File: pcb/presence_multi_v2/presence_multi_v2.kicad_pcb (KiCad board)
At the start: 2 copper layers, 77 x 42 mm, 32 parts, among them IC1 LDL1117S33R, J1 USB_C_Receptacle_USB2.0_16P, J2 TC2050, J3 Conn_01x06_Socket, U3 CH340E, Y1 Wurth 830050789

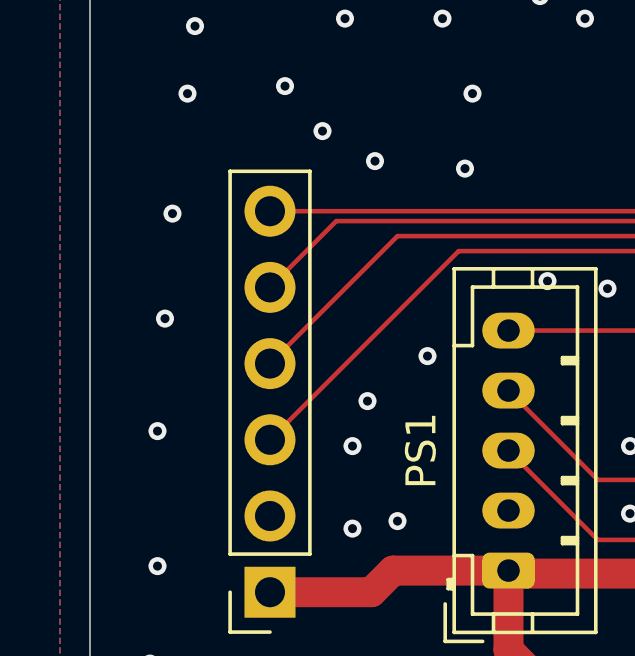
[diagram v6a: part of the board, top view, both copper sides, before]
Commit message: added info on components to a silkscreen
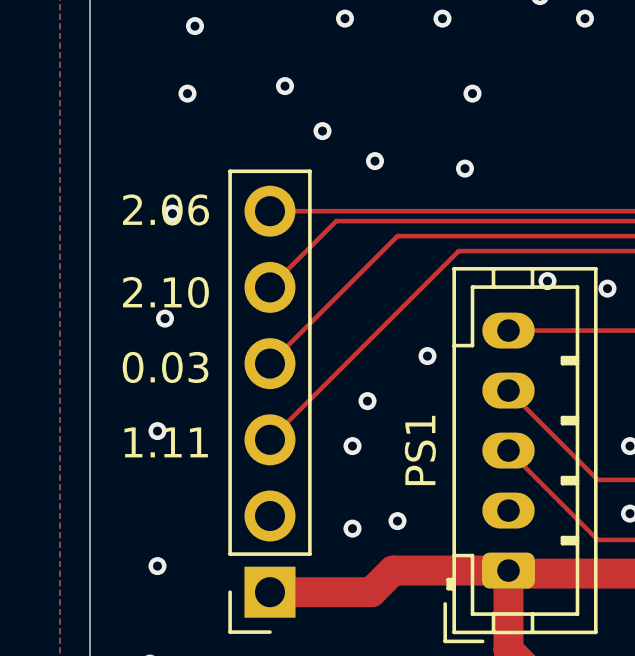
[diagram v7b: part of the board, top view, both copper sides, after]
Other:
- board text added: "0.03"
- board text added: "1.11"
- board text added: "2.06"
- board text added: "2.10"
- board text added: "C1,C4,C5:10u C2,C3,C6,C7:470n D1: USBLC6-2SC6 IC1: LDL1117S33R R1: 0 R2,R3: 5k1 R4: 180 U3: CH340E"
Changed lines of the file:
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@@
 		(layer "Edge.Cuts")
+	)
+	(gr_text "2.10"
+		(at 88 106.75 0)
+		(layer "F.SilkS")
+		(effects
+			(font
+				(size 1 1)
+				(thickness 0.15)
+			)
+			(justify left bottom)
+		)
+	)
+	(gr_text "1.11"
+		(at 88 111.75 0)
+		(layer "F.SilkS")
+		(effects
+			(font
+				(size 1 1)
+				(thickness 0.15)
+			)
+			(justify left bottom)
+		)
+	)
+	(gr_text "2.06"
+		(at 88 104 0)
+		(layer "F.SilkS")
+		(effects
+			(font
+				(size 1 1)
+				(thickness 0.15)
+			)
+			(justify left bottom)
+		)
+	)
+	(gr_text "0.03"
+		(at 88 109.25 0)
+		(layer "F.SilkS")
+		(effects
+			(font
+				(size 1 1)
+				(thickness 0.15)
+			)
+			(justify left bottom)
+		)
+	)
+	(gr_text "C1,C4,C5:10u\nC2,C3,C6,C7:470n\nD1: USBLC6-2SC6\nIC1: LDL1117S33R\nR1: 0\nR2,R3: 5k1\nR4: 180\nU3: CH340E"
+		(at 151 102 0)
+		(layer "B.SilkS")
+		(effects
+			(font
+				(size 1 1)
+				(thickness 0.15)
+			)
+			(justify left bottom mirror)
+		)
 	)
 	(segment

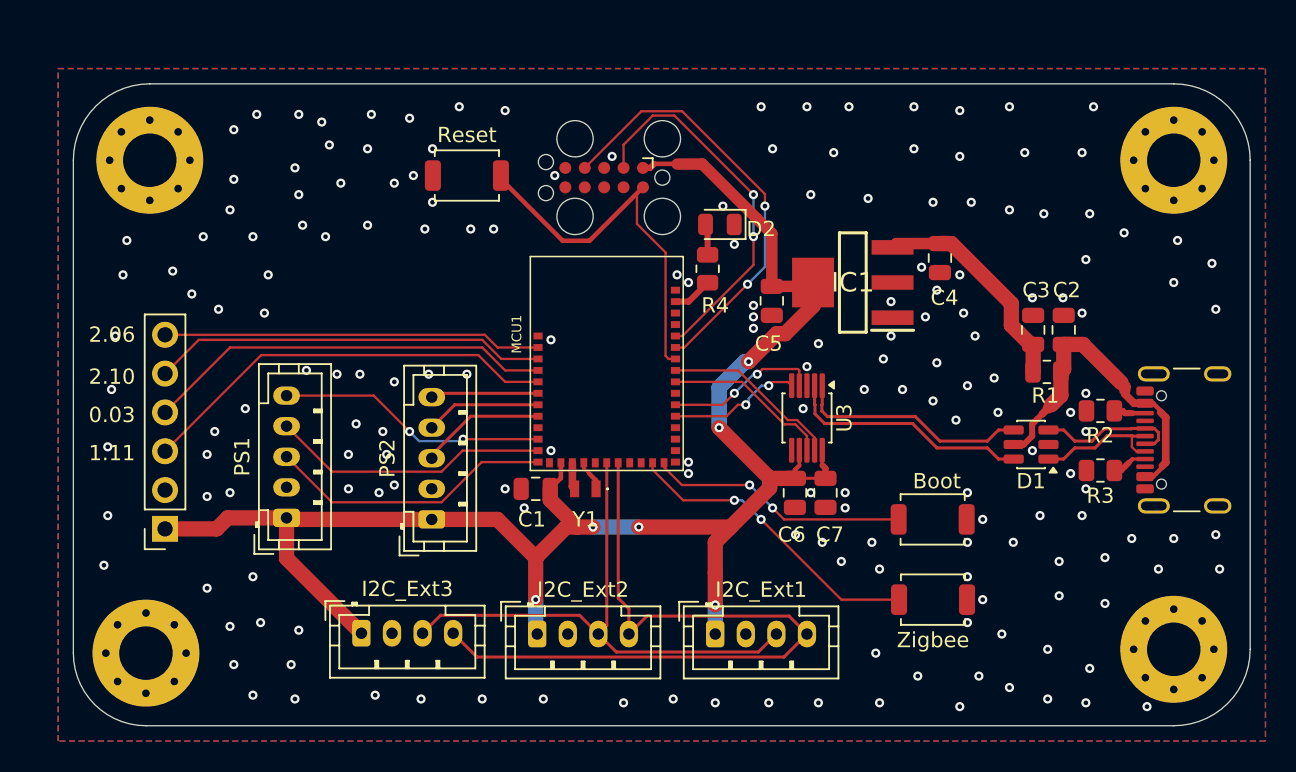
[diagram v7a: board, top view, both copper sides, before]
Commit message: PCB: re-arranged the whole board
made it significantly smaller
used a slightly different footprint for buttons
USB-C should be placed symmetrically now
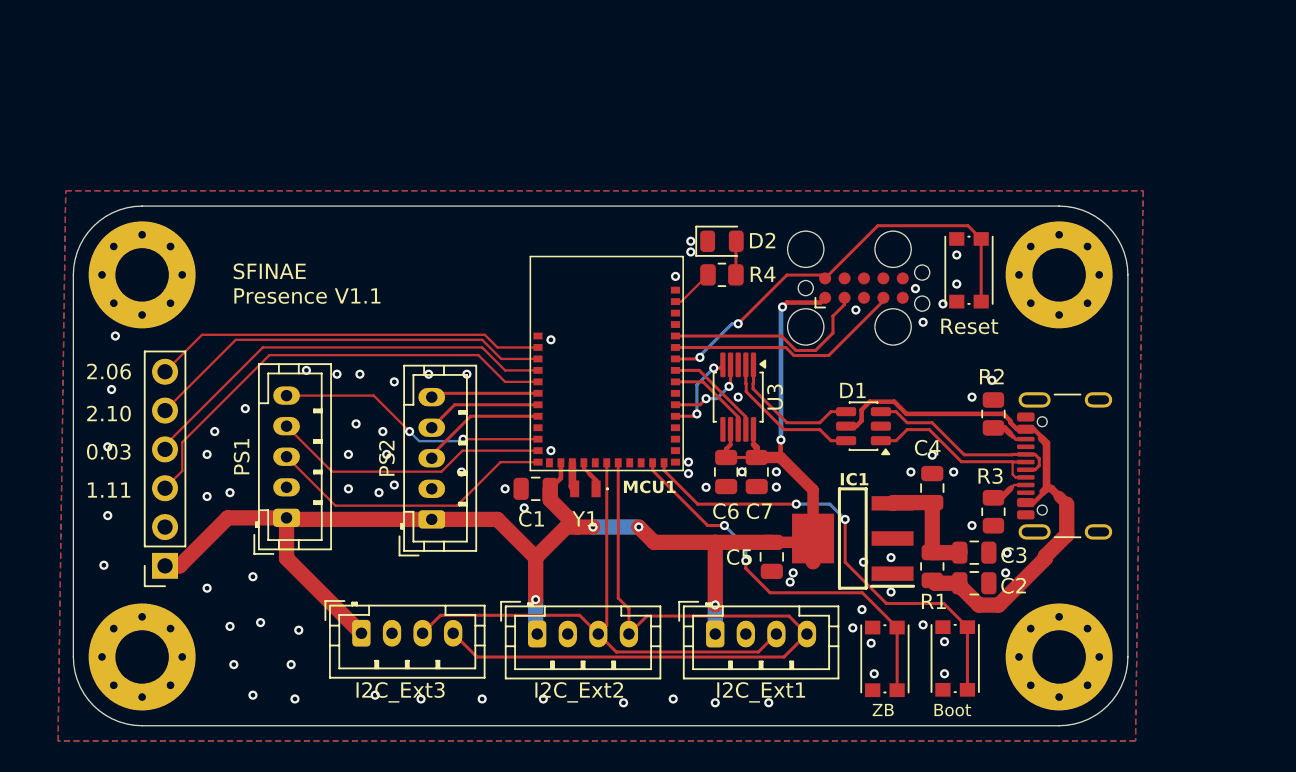
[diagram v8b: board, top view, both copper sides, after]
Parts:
- Boot, Reset: footprint Button_Switch_SMD:SW_SPST_TS-1088-xR020 -> Button_Switch_SMD:SW_Push_1P1T_NO_CK_KMR2
- ZB: renamed from Zigbee; footprint Button_Switch_SMD:SW_SPST_TS-1088-xR020 -> Button_Switch_SMD:SW_Push_1P1T_NO_CK_KMR2
- moved Reset 33.4 mm to (145.6, 99.2), turned to 90 degrees
- moved J2 18.5 mm to (138.7, 100.4), turned to 0 degrees
- moved C2 17.6 mm to (145.9, 119.7), turned to 0 degrees
- moved C5 16.8 mm to (132.7, 118.0)
- moved IC1 16.8 mm to (138.0, 116.8)
- moved C3 15.1 mm to (145.9, 117.7), turned to 0 degrees
- moved C4 15.1 mm to (143.2, 113.5), turned to -90 degrees
- moved R1 14.8 mm to (143.2, 118.6), turned to 90 degrees
- moved D1 11.0 mm to (138.7, 109.4)
- moved MH2 10.6 mm to (151.5, 99.5)
- moved Boot 9.22 mm to (144.7, 124.6), turned to 90 degrees
- moved J1 7.98 mm to (153.0, 112.0)
- moved MH1 7.52 mm to (151.5, 124.5)
- moved MH3 7.52 mm to (91.5, 99.5)
- moved R3 7.50 mm to (147.2, 115.0), turned to -90 degrees
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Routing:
- net +VBUS: track 22.0 -> 35.5 mm
- net /BTN_MCUBoot: track 17.1 -> 30.3 mm
- net /SWDCLK: track 28.4 -> 15.5 mm, vias 2 -> 0
- net +3V3: track 112.5 -> 100.8 mm
- net /SWDIO: track 24.6 -> 13.8 mm, vias 2 -> 0
- net /LDO_IN: track 14.7 -> 7.87 mm
- net /USBD-: track 16.1 -> 9.63 mm
- net /USBD+: track 15.3 -> 8.89 mm
- net /BTN_ZB: track 20.1 -> 25.7 mm
- net /UART00_RX: track 11.0 -> 5.87 mm
- net /UART00_TX: track 11.8 -> 6.68 mm
- net /UART00_CTS: track 10.1 -> 5.45 mm
- net /USBCD-: track 8.66 -> 12.4 mm
- net /USBCD+: track 9.40 -> 13.1 mm
- net /UART00_RTS: track 8.76 -> 5.61 mm
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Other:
- board size 77 x 42 mm -> 69 x 34 mm
- board text added: "SFINAE Presence V1.1"
